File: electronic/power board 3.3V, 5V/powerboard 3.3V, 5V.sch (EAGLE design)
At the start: 10 parts, among them IC1_5V REG1117, IC2_3.3V REG1117, X1 GND, X3_5V 5V, X4_3.3V 3.3V, X5 IN

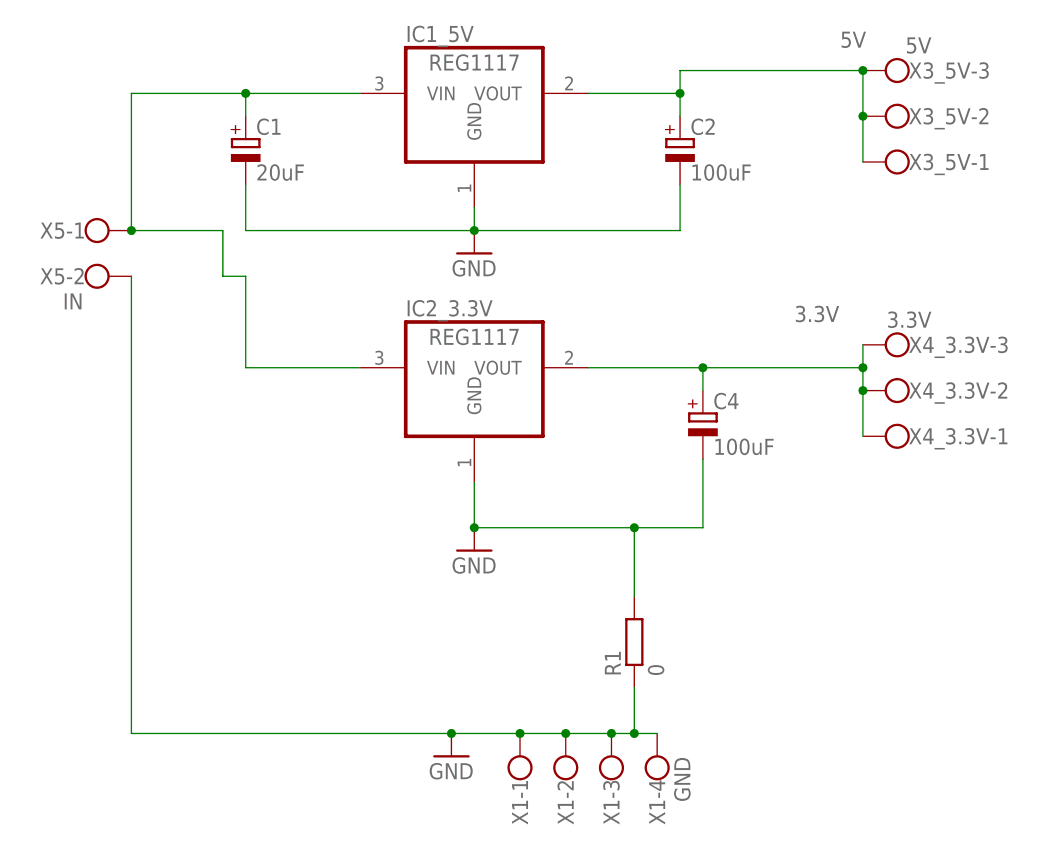
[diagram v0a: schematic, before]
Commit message: moved schematics to the KiCad
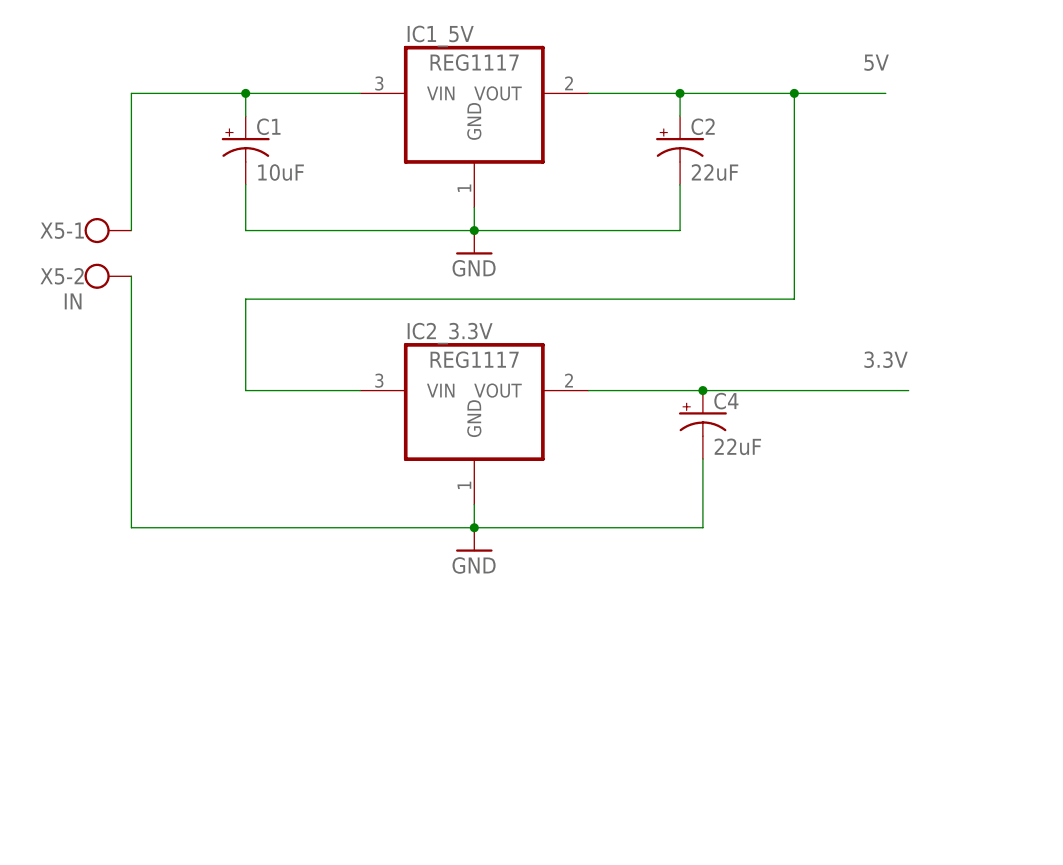
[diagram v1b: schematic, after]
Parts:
- removed R1: 0, resistor:R-EU_0204/5
- removed X1: GND, con-wago-500:W237-4
- removed X3_5V: 5V, con-wago-500:W237-103
- removed X4_3.3V: 3.3V, con-wago-500:W237-103
- C1: value 20uF -> 10uF; device resistor:CPOL-EUE3.5-8 -> SparkFun-Capacitors:10UF-POLAR-EIA3216-16V-10%(TANT)
- C2, C4: value 100uF -> 22uF; device resistor:CPOL-EUE3.5-8 -> SparkFun-Capacitors:10UF-POLAR-EIA3528-20V-10%(TANT)
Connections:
- net 3.3V: no longer X4_3.3V-1.KL, X4_3.3V-2.KL, X4_3.3V-3.KL
- net 5V: now also IC2_3.3V.VIN; no longer X3_5V-1.KL, X3_5V-2.KL, X3_5V-3.KL
- net GND: no longer R1.1, R1.2, X1-1.KL, X1-2.KL, X1-3.KL, X1-4.KL
- net VIN: no longer IC2_3.3V.VIN
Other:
- moved on the sheet: IC2_3.3V
